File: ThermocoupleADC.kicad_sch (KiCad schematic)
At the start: 22 parts, among them U12 ADS112C04

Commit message: grounded usb-c receptacle shield
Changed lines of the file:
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@@
 		(dnp no)
 		(property "Reference" "C43"
-			(at 150.114 42.164 90)
+			(at 151.638 39.37 0)
 			(effects
 				(font
@@
 		)
 		(property "Value" "10nF"
-			(at 148.082 42.672 90)
+			(at 152.146 41.656 0)
 			(effects
 				(font
@@
 		(dnp no)
 		(property "Reference" "C47"
-			(at 150.114 78.994 90)
+			(at 151.13 76.2 0)
 			(effects
 				(font
@@
 		)
 		(property "Value" "10nF"
-			(at 148.082 79.502 90)
+			(at 151.638 78.232 0)
 			(effects
 				(font
@@
 		(dnp no)
 		(property "Reference" "C49"
-			(at 150.114 94.234 90)
+			(at 151.384 91.44 0)
 			(effects
 				(font
@@
 		)
 		(property "Value" "10nF"
-			(at 148.082 94.742 90)
+			(at 151.892 93.726 0)
 			(effects
 				(font
@@
 		(dnp no)
 		(property "Reference" "C44"
-			(at 150.114 57.404 90)
+			(at 151.638 55.118 0)
 			(effects
 				(font
@@
 		)
 		(property "Value" "10nF"
-			(at 148.082 57.912 90)
-			(effects
-				(font
+			(at 152.4 57.404 0)
+			(effects
+				(font

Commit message: add 2 stage lockout to ignitor, add ignitor resistance reading with adc current source
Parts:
- renumbered C45 to C35, C46 to C36, C43 to C37, C42 to C38, C44 to C39, C47 to C40, C48 to C41, C49 to C42, D13 to D21, D32 to D22, D36 to D23, D34 to D24, R82 to R48, R76 to R49, R77 to R50, R60 to R51, R66 to R52, R36 to R53, R75 to R54, R80 to R55, R81 to R56, U12 to U10

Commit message: add capacitor and resistor footprints
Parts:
- removed C38, C41: 100nF, Capacitor_SMD:C_0805_2012Metric, symbol Device:C_Small
- removed C39, C40: 10nF, Capacitor_SMD:C_0805_2012Metric, symbol Device:C_Small
- added C43, C44, C46: 10nF, Capacitor_SMD:C_0603_1608Metric, symbol Device:C_Small
- added C45: 0.1μF, Capacitor_SMD:C_0402_1005Metric, symbol Device:C_Small
- C39: renamed from C35; LCSC C1525 -> C307331
- C40: renamed from C36; LCSC C1525 -> C307331
- C41: renamed from C37; footprint Capacitor_SMD:C_0805_2012Metric -> Capacitor_SMD:C_0603_1608Metric; LCSC (none) -> C5299898
- C42: value 10nF -> 0.1μF; footprint Capacitor_SMD:C_0805_2012Metric -> Capacitor_SMD:C_0402_1005Metric; LCSC (none) -> C307331; MPN (none) -> CL05B104KO5NNNC
- D17: renamed from D21; LCSC (none) -> C83575
- D18: renamed from D22; LCSC (none) -> C83575
- D19: renamed from D23; LCSC (none) -> C83575
- D20: renamed from D24; LCSC (none) -> C83575
- U10: ADC Number 1 -> (none); I2C Address 100 0000 -> (none)
- renumbered R48 to R46, R49 to R47, R50 to R48, R51 to R49, R52 to R50, R53 to R51, R54 to R52, R55 to R53, R56 to R54
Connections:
- net AIN0: now also C45.1, C46.1; no longer C42.1
- net AIN1: now also C44.2, C45.2
- net AIN2: now also C42.1, C43.1
- net AIN3: now also C42.2
- net GND: now also C43.2, C44.1, C46.2; no longer C42.2

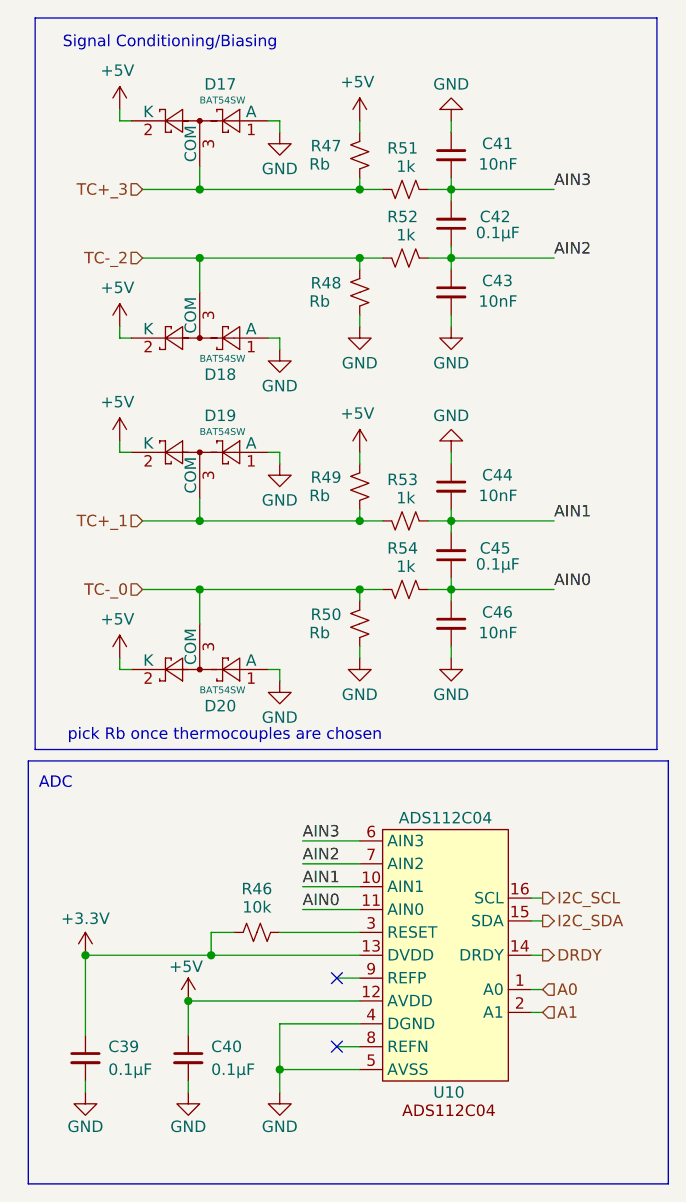
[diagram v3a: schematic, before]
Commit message: change connectors and more progress on pcb
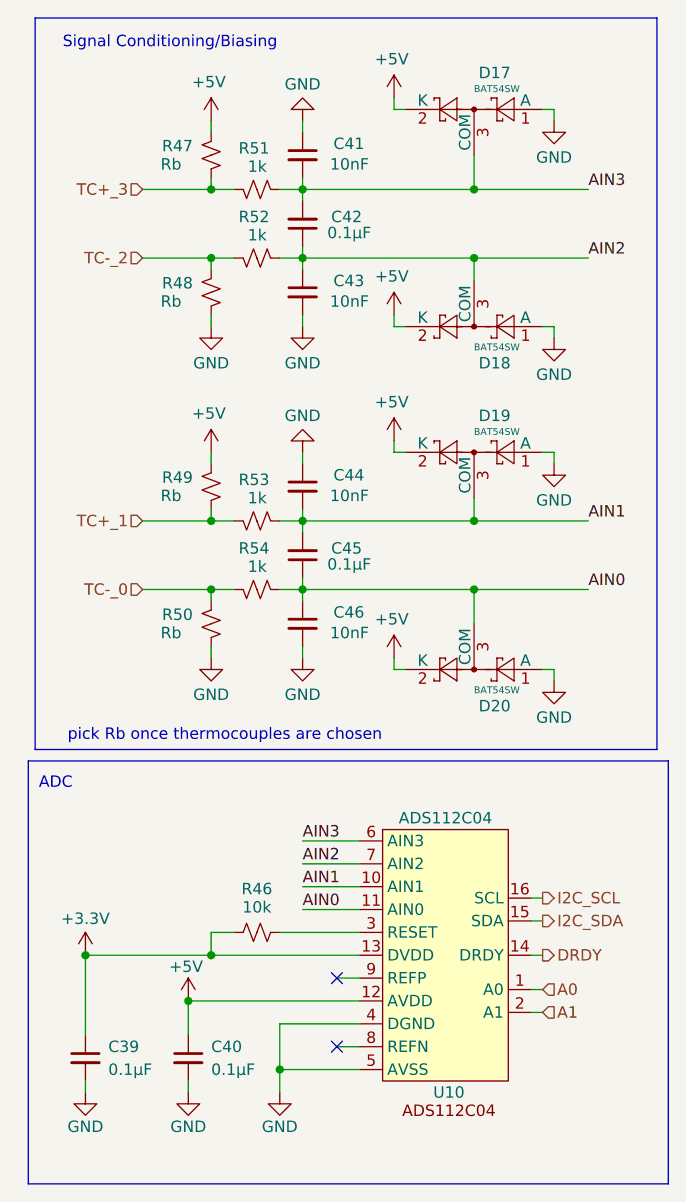
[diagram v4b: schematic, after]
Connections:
- net AIN0: now also D20.3 (COM)
- net AIN1: now also D19.3 (COM)
- net AIN2: now also D18.3 (COM)
- net AIN3: now also D17.3 (COM)
- net TC+_1: no longer D19.3 (COM)
- net TC+_3: no longer D17.3 (COM)
- net TC-_0: no longer D20.3 (COM)
- net TC-_2: no longer D18.3 (COM)
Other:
- moved on the sheet: C41, C42, C43, C44, C45, C46, D17, D18, D19, D20, R47, R48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

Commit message: change clamping resistors on tc adcs for lower leakage current
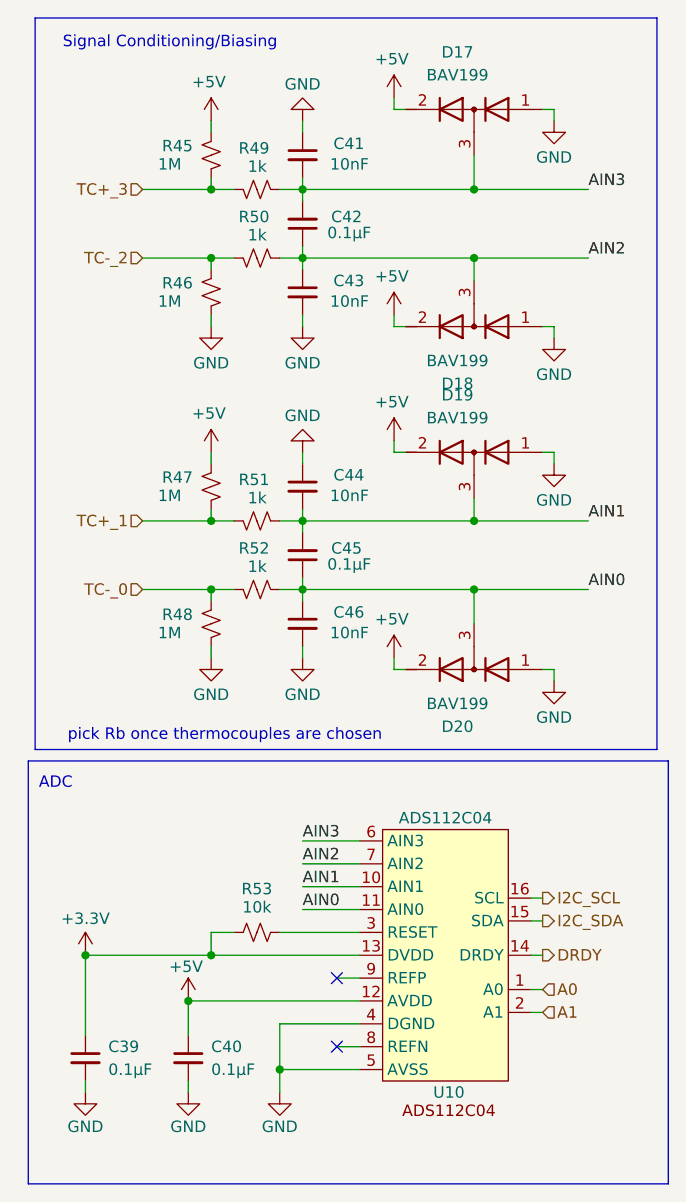
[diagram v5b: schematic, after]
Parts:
- removed D17, D18, D19, D20: BAT54SW, Package_TO_SOT_SMD:SOT-323_SC-70, symbol Diode:BAT54SW
- added D17, D18, D19, D20: BAV199, Package_TO_SOT_SMD:SOT-23, symbol Device:D_Dual_Series_AKC
- R45: renamed from R47; value Rb -> 1M
- R46: renamed from R48; value Rb -> 1M
- R47: renamed from R49; value Rb -> 1M
- R48: renamed from R50; value Rb -> 1M
- renumbered R51 to R49, R52 to R50, R53 to R51, R54 to R52, R46 to R53
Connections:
- net +5V: now also D17.2 (K), D18.2 (K), D19.2 (K), D20.2 (K)
- net AIN0: now also D20.3 (common)
- net AIN1: now also D19.3 (common)
- net AIN2: now also D18.3 (common)
- net AIN3: now also D17.3 (common)
- net GND: now also D17.1 (A), D18.1 (A), D19.1 (A), D20.1 (A)

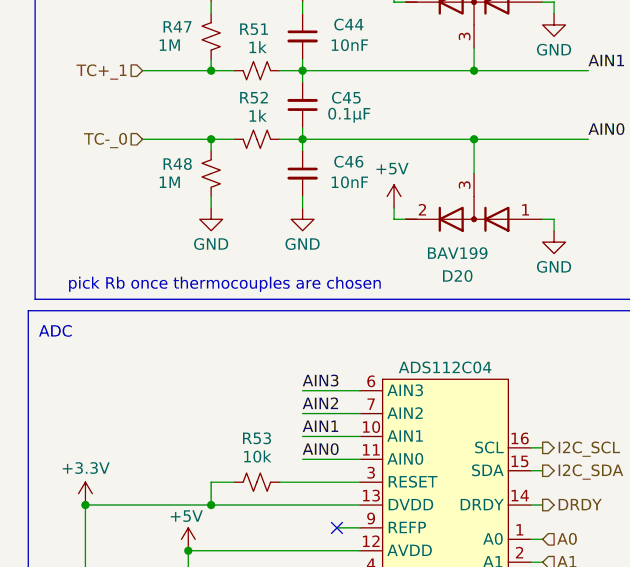
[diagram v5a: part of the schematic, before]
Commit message: add silkscreen labels to connectors, remove pick Rb message (was already chosen)
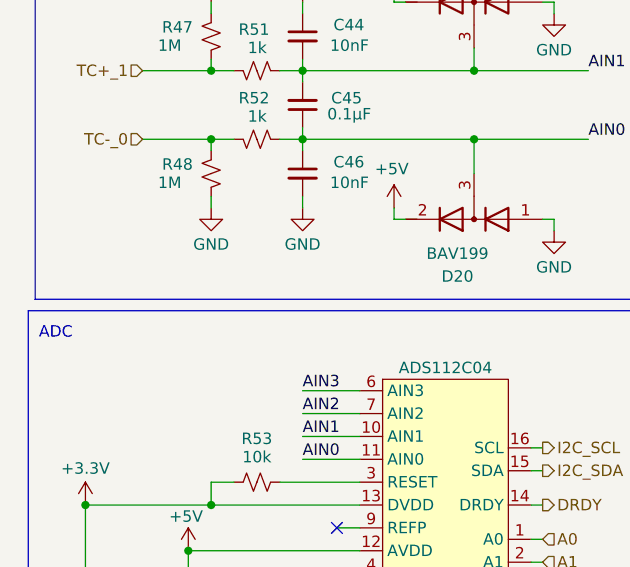
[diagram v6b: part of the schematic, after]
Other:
- note removed: "pick Rb once thermocouples are chosen"
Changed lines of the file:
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@@
-		)
-	)
-	(text "pick Rb once thermocouples are chosen"
-		(exclude_from_sim no)
-		(at 119.634 105.156 0)
-		(effects
-			(font
-				(size 1.27 1.27)
-			)
 		)
 	)

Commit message: Update version number in KiCad files
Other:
- company: (none) -> Queen's Rocket Engineering Team
- title: (none) -> PANDA
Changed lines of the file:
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@@
 	(generator_version "9.0")
 	(paper "A4")
+	(title_block
+		(title "PANDA")
+		(date "2025-12-21")
+		(rev "3.0.0")
+		(company "Queen's Rocket Engineering Team")
+	)
 	(rectangle
 		(start 97.79 107.95)
